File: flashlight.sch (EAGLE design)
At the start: 2 parts

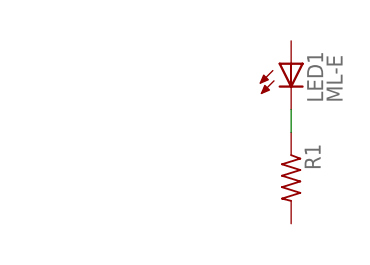
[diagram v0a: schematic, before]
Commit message: top board rev 3 (with the 350ma reg)
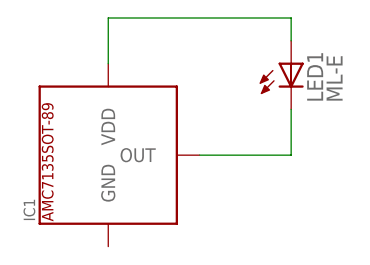
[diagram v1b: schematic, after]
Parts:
- removed R1: (no value), resistor:R-US_R2010
- added IC1: AMC7135SOT-89, esoteric-regulators:AMC7135SOT-89
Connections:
- new net N$28: IC1.VDD, LED1G$1.A@1
- net N$3: now also IC1.OUT; no longer R1.1
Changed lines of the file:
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@@
 <?xml version="1.0" encoding="utf-8"?>
 <!DOCTYPE eagle SYSTEM "eagle.dtd">
-<eagle version="7.1.0">
+<eagle version="7.2.0">
 <drawing>
 <settings>
@@
 <setting verticaltext="up"/>
 </settings>
-<grid distance="0.1" unitdist="inch" unit="inch" style="lines" multiple="1" display="yes" altdistance="0.01" altunitdist="inch" altunit="inch"/>
+<grid distance="0.1" unitdist="inch" unit="inch" style="lines" multiple="1" display="no" altdistance="0.01" altunitdist="inch" altunit="inch"/>
 <layers>
 <layer number="1" name="Top" color="4" fill="1" visible="no" active="no"/>
@@
 </classes>
 <parts>
-<part name="R1" library="resistor" deviceset="R-US_" device="R2010"/>
 <part name="LED1" library="led" deviceset="ML-E" device=""/>
+<part name="IC1" library="esoteric-regulators" deviceset="AMC7135" device="SOT-89"/>
 </parts>
 <sheets>
@@
 </plain>
 <instances>
-<instance part="R1" gate="G$1" x="38.1" y="33.02" rot="R270"/>
 <instance part="LED1" gate="G$1" x="38.1" y="43.18"/>
+<instance part="IC1" gate="G$1" x="10.16" y="27.94"/>
 </instances>
 <busses>
@@
 <net name="N$3" class="0">
 <segment>
-<pinref part="R1" gate="G$1" pin="1"/>
-<wire x1="38.1" y1="40.64" x2="38.1" y2="38.1" width="0.1524" layer="91"/>
 <pinref part="LED1" gate="G$1" pin="C@1"/>
+<wire x1="38.1" y1="40.64" x2="38.1" y2="35.56" width="0.1524" layer="91"/>
+<pinref part="IC1" gate="G$1" pin="OUT"/>
+<wire x1="38.1" y1="35.56" x2="27.94" y2="35.56" width="0.1524" layer="91"/>
 </segment>
 </net>
+<net name="N$28" class="0">
+<segment>
+<pinref part="LED1" gate="G$1" pin="A@1"/>
+<wire x1="38.1" y1="48.26" x2="38.1" y2="50.8" width="0.1524" layer="91"/>
+<pinref part="IC1" gate="G$1" pin="VDD"/>
+<wire x1="38.1" y1="50.8" x2="17.78" y2="50.8" width="0.1524" layer="91"/>
+<wire x1="17.78" y1="50.8" x2="17.78" y2="45.72" width="0.1524" layer="91"/>
+</segment>
+</net>
